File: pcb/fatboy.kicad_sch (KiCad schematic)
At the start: 76 parts, among them SW1 SW_Push, U1 Helios

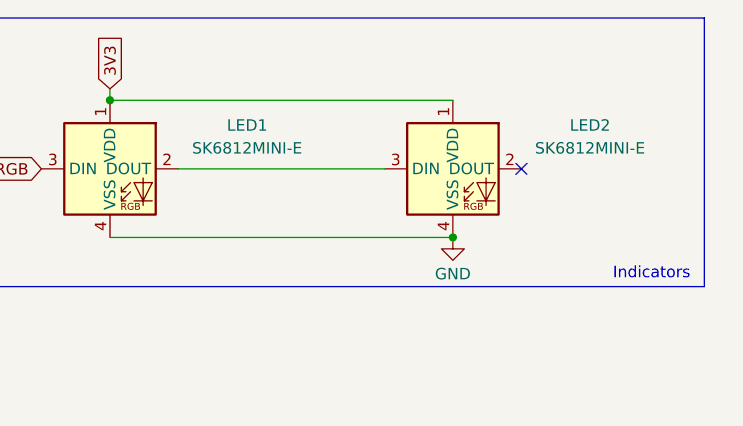
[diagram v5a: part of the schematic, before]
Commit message: update to use PCM_marbastlib:LED6028R
Signed-off-by: Anant Thazhemadam <anant.thazhemadam@gmail.com>
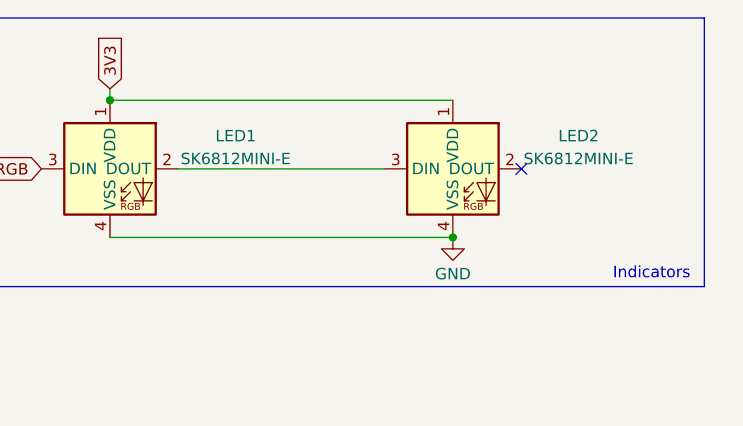
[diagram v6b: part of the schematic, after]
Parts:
- removed LED1, LED2: SK6812MINI-E, fatboy:LED_6028R, symbol marbastlib-various:SK6812MINI-E
- added LED1, LED2: SK6812MINI-E, PCM_marbastlib-various:LED_6028R, symbol PCM_marbastlib-various:SK6812MINI-E
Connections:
- net 3V3: now also LED1.1 (VDD), LED2.1 (VDD)
- net GND: now also LED1.4 (VSS), LED2.4 (VSS)
- net RGB: now also LED1.3 (DIN)
- new net: LED1.2 (DOUT), LED2.3 (DIN)
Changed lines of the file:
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@@
 	)
 	(junction
+		(at 160.02 36.83)
+		(diameter 0)
+		(color 0 0 0 0)
+	)
+	(junction
 		(at 107.95 171.45)
 		(diameter 0)
@@
 	)
 	(junction
-		(at 121.92 21.59)
-		(diameter 0)
-		(color 0 0 0 0)
-	)
-	(junction
 		(at 57.15 133.35)
 		(diameter 0)
@@
 	)
 	(junction
+		(at 121.92 21.59)
+		(diameter 0)
+		(color 0 0 0 0)
+	)
+	(junction
 		(at 120.65 190.5)
 		(diameter 0)
@@
 	)
 	(junction
-		(at 160.02 36.83)
-		(diameter 0)
-		(color 0 0 0 0)
-	)
-	(junction
 		(at 146.05 152.4)
 		(diameter 0)
@@
 	)
 	(no_connect
-		(at 167.64 29.21)
-	)
-	(no_connect
 		(at 50.8 31.75)
 	)
@@
 	)
 	(no_connect
+		(at 167.64 29.21)
+	)
+	(no_connect
 		(at 40.64 69.85)
 	)
@@
 	(wire
 		(pts
-			(xy 121.92 21.59) (xy 160.02 21.59)
-		)
-		(stroke
-			(width 0)
-			(type default)
-		)
-	)
-	(wire
-		(pts
 			(xy 57.15 190.5) (xy 69.85 190.5)
 		)
@@
 	(wire
 		(pts
-			(xy 121.92 36.83) (xy 160.02 36.83)
-		)
-		(stroke
-			(width 0)
-			(type default)
-		)
-	)
-	(wire
-		(pts
 			(xy 69.85 133.35) (xy 82.55 133.35)
 		)
@@
 	(wire
 		(pts
+			(xy 121.92 36.83) (xy 160.02 36.83)
+		)
+		(stroke
+			(width 0)
+			(type default)
+		)
+	)
+	(wire
+		(pts
 			(xy 44.45 133.35) (xy 57.15 133.35)
 		)
@@
 	(wire
 		(pts
+			(xy 129.54 29.21) (xy 152.4 29.21)
+		)
+		(stroke
+			(width 0)
+			(type default)
+		)
+	)
+	(wire
+		(pts
 			(xy 120.65 171.45) (xy 133.35 171.45)
 		)
@@
 	(wire
 		(pts
-			(xy 129.54 29.21) (xy 152.4 29.21)
+			(xy 153.67 114.3) (xy 153.67 120.65)
 		)
 		(stroke
@@
 	(wire
 		(pts
-			(xy 153.67 114.3) (xy 153.67 120.65)
+			(xy 133.35 152.4) (xy 146.05 152.4)
 		)
 		(stroke
@@
 	(wire
 		(pts
-			(xy 133.35 152.4) (xy 146.05 152.4)
+			(xy 57.15 133.35) (xy 69.85 133.35)
 		)
 		(stroke
@@
 	(wire
 		(pts
-			(xy 57.15 133.35) (xy 69.85 133.35)
+			(xy 121.92 21.59) (xy 160.02 21.59)
 		)
 		(stroke
@@
 	)
 	(symbol
+		(lib_id "PCM_marbastlib-various:SK6812MINI-E")
+		(at 160.02 29.21 0)
+		(unit 1)
+		(exclude_from_sim no)
+		(in_bom yes)
+		(on_board yes)
+		(dnp no)
+		(fields_autoplaced yes)
+		(property "Reference" "LED2"
+			(at 173.99 25.562 0)
+			(effects
+				(font
+					(size 1.27 1.27)
+				)
+			)
+		)
+		(property "Value" "SK6812MINI-E"
+			(at 173.99 28.102 0)
+			(effects
+				(font
+					(size 1.27 1.27)
+				)
+			)
+		)
+		(property "Footprint" "PCM_marbastlib-various:LED_6028R"
+			(at 160.02 29.21 0)
+			(effects
+				(font
+					(size 1.27 1.27)
+				)
+				(hide yes)
+			)
+		)
+		(property "Datasheet" ""
+			(at 160.02 29.21 0)
+			(effects
+				(font
+					(size 1.27 1.27)
+				)
+				(hide yes)
+			)
+		)
+		(property "Description" "Reverse mount adressable LED (WS2812 protocol)"
+			(at 160.02 29.21 0)
+			(effects
+				(font
+					(size 1.27 1.27)
+				)
+				(hide yes)
+			)
+		)
+		(pin "4"
+		)
+		(pin "1"
+		)
+		(pin "2"
+		)
+		(pin "3"
+		)
+		(instances
+			(project "fatboy"
+				(path "/ebfc642c-0c68-4d3e-b71f-85668561aa10"
+					(reference "LED2")
+					(unit 1)
+				)
+			)
+		)
+	)
+	(symbol
 		(lib_id "Diode:1N4148W")
 		(at 69.85 186.69 90)
@@
 	)
 	(symbol
-		(lib_id "marbastlib-various:SK6812MINI-E")
-		(at 160.02 29.21 0)
-		(unit 1)
-		(exclude_from_sim no)
-		(in_bom yes)
-		(on_board yes)
-		(dnp no)
-		(property "Reference" "LED2"
-			(at 175.26 24.384 0)
-			(effects
-				(font
-					(size 1.27 1.27)
-				)
-			)
-		)
-		(property "Value" "SK6812MINI-E"
-			(at 175.26 26.924 0)
-			(effects
-				(font
-					(size 1.27 1.27)
-				)
-			)
-		)
-		(property "Footprint" "fatboy:LED_6028R"
-			(at 160.02 29.21 0)
-			(effects
-				(font
-					(size 1.27 1.27)
-				)
-				(hide yes)
-			)
-		)
-		(property "Datasheet" ""
-			(at 160.02 29.21 0)
-			(effects
-				(font
-					(size 1.27 1.27)
-				)
-				(hide yes)
-			)
-		)
-		(property "Description" ""
-			(at 160.02 29.21 0)
-			(effects
-				(font
-					(size 1.27 1.27)
-				)
-				(hide yes)
-			)
-		)
-		(pin "2"
-		)
-		(pin "4"
-		)
-		(pin "1"
-		)
-		(pin "3"
-		)
-		(instances
-			(project "fatboy"
-				(path "/ebfc642c-0c68-4d3e-b71f-85668561aa10"
-					(reference "LED2")
-					(unit 1)
-				)
-			)
-		)
-	)
-	(symbol
 		(lib_id "PCM_marbastlib-mx:MX_SW_HS_CPG151101S11")
 		(at 54.61 142.24 0)
@@
 	)
 	(symbol
-		(lib_id "marbastlib-various:SK6812MINI-E")
-		(at 121.92 29.21 0)
-		(unit 1)
-		(exclude_from_sim no)
-		(in_bom yes)
-		(on_board yes)
-		(dnp no)
-		(property "Reference" "LED1"
-			(at 137.16 24.384 0)
-			(effects
-				(font
-					(size 1.27 1.27)
-				)
-			)
-		)
-		(property "Value" "SK6812MINI-E"
-			(at 137.16 26.924 0)
-			(effects
-				(font
-					(size 1.27 1.27)
-				)
-			)
-		)
-		(property "Footprint" "fatboy:LED_6028R"
-			(at 121.92 29.21 0)
-			(effects
-				(font
-					(size 1.27 1.27)
-				)
-				(hide yes)
-			)
-		)
-		(property "Datasheet" ""
-			(at 121.92 29.21 0)
-			(effects
-				(font
-					(size 1.27 1.27)
-				)
-				(hide yes)
-			)
-		)
-		(property "Description" ""
-			(at 121.92 29.21 0)
-			(effects
-				(font
-					(size 1.27 1.27)
-				)
-				(hide yes)
-			)
-		)
-		(pin "2"
-		)
-		(pin "4"
-		)
-		(pin "1"
-		)
-		(pin "3"
-		)
-		(instances
-			(project "fatboy"
-				(path "/ebfc642c-0c68-4d3e-b71f-85668561aa10"
-					(reference "LED1")
-					(unit 1)
-				)
-			)
-		)
-	)
-	(symbol
 		(lib_id "PCM_marbastlib-mx:MX_SW_HS_CPG151101S11")
 		(at 41.91 161.29 0)
@@
 					(unit 1)
 				)
+			)
+		)
+	)
+	(symbol
+		(lib_id "PCM_marbastlib-various:SK6812MINI-E")
+		(at 121.92 29.21 0)
+		(unit 1)
+		(exclude_from_sim no)
+		(in_bom yes)
+		(on_board yes)
+		(dnp no)
+		(fields_autoplaced yes)
+		(property "Reference" "LED1"
+			(at 135.89 25.562 0)
+			(effects
+				(font
+					(size 1.27 1.27)
+				)
+			)
+		)
+		(property "Value" "SK6812MINI-E"
+			(at 135.89 28.102 0)
+			(effects
+				(font
+					(size 1.27 1.27)
+				)
+			)
+		)
+		(property "Footprint" "PCM_marbastlib-various:LED_6028R"
+			(at 121.92 29.21 0)
+			(effects
+				(font
+					(size 1.27 1.27)
+				)
+				(hide yes)
+			)
+		)
+		(property "Datasheet" ""
+			(at 121.92 29.21 0)
+			(effects
+				(font
+					(size 1.27 1.27)
+				)
+				(hide yes)
+			)
+		)
+		(property "Description" "Reverse mount adressable LED (WS2812 protocol)"
+			(at 121.92 29.21 0)
+			(effects
+				(font
+					(size 1.27 1.27)
+				)
+				(hide yes)
+			)
+		)
+		(pin "4"
+		)
+		(pin "1"
+		)
+		(pin "2"
+		)
+		(pin "3"
+		)
+		(instances
+			(project "fatboy"
+				(path "/ebfc642c-0c68-4d3e-b71f-85668561aa10"
+					(reference "LED1")
+					(unit 1)
+				)

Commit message: update helios footprint
Signed-off-by: Anant Thazhemadam <anant.thazhemadam@gmail.com>
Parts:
- removed U1: Helios, PCM_marbastlib-xp-promicroish:Helios_ACH, symbol marbastlib-promicroish:Helios
- added U1: Helios, PCM_marbastlib-xp-promicroish:Helios_AH_USBup, symbol PCM_marbastlib-promicroish:Helios
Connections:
- net 3V3: now also U1.16 (3V3)
- net 5V: now also U1.13 (5V)
- net COL1: now also U1.21 (P22)
- net COL10: now also U1.9 (P6)
- net COL2: now also U1.20 (P26)
- net COL3: now also U1.19 (P27)
- net COL4: now also U1.18 (P28)
- net COL5: now also U1.17 (P29)
- net COL6: now also U1.5 (P2)
- net COL7: now also U1.6 (P3)
- net COL8: now also U1.7 (P4)
- net COL9: now also U1.8 (P5)
- net GND: now also U1.14 (GND), U1.3 (GND), U1.4 (GND)
- net RESET: now also U1.15 (RST)
- net RGB: now also U1.29 (P16)
- net ROW1: now also U1.10 (P7)
- net ROW2: now also U1.11 (P8)
- net ROW3: now also U1.12 (P9)
- net ROW4: now also U1.25 (P12)
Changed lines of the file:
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@@
+	)
+	(symbol
+		(lib_id "PCM_marbastlib-promicroish:Helios")
+		(at 38.1 48.26 0)
+		(unit 1)
+		(exclude_from_sim no)
+		(in_bom no)
+		(on_board yes)
+		(dnp no)
+		(fields_autoplaced yes)
+		(property "Reference" "U1"
+			(at 41.5641 24.13 0)
+			(effects
+				(font
+					(size 1.27 1.27)
+				)
+				(justify left)
+			)
+		)
+		(property "Value" "Helios"
+			(at 41.5641 26.67 0)
+			(effects
+				(font
+					(size 1.27 1.27)
+				)
+				(justify left)
+			)
+		)
+		(property "Footprint" "PCM_marbastlib-xp-promicroish:Helios_AH_USBup"
+			(at 38.1 72.39 0)
+			(effects
+				(font
+					(size 1.27 1.27)
+				)
+				(hide yes)
+			)
+		)
+		(property "Datasheet" "https://github.com/0xCB-dev/0xCB-Helios"
+			(at 38.1 74.93 0)
+			(effects
+				(font
+					(size 1.27 1.27)
+				)
+				(hide yes)
+			)
+		)
+		(property "Description" "Symbol for an 0xCB Helios"
+			(at 38.1 48.26 0)
+			(effects
+				(font
+					(size 1.27 1.27)
+				)
+				(hide yes)
+			)
+		)
+		(pin "10"
+		)
+		(pin "17"
+		)
+		(pin "21"
+		)
+		(pin "22"
+		)
+		(pin "2"
+		)
+		(pin "20"
+		)
+		(pin "18"
+		)
+		(pin "14"
+		)
+		(pin "12"
+		)
+		(pin "5"
+		)
+		(pin "6"
+		)
+		(pin "26"
+		)
+		(pin "27"
+		)
+		(pin "28"
+		)
+		(pin "29"
+		)
+		(pin "30"
+		)
+		(pin "31"
+		)
+		(pin "32"
+		)
+		(pin "33"
+		)
+		(pin "34"
+		)
+		(pin "11"
+		)
+		(pin "19"
+		)
+		(pin "23"
+		)
+		(pin "24"
+		)
+		(pin "3"
+		)
+		(pin "4"
+		)
+		(pin "1"
+		)
+		(pin "9"
+		)
+		(pin "13"
+		)
+		(pin "16"
+		)
+		(pin "25"
+		)
+		(pin "15"
+		)
+		(pin "7"
+		)
+		(pin "8"
+		)
+		(instances
+			(project "fatboy"
+				(path "/ebfc642c-0c68-4d3e-b71f-85668561aa10"
+					(reference "U1")
+					(unit 1)
+				)
+			)
+		)
 	)
 	(symbol
@@
 					(unit 1)
 				)
-			)
-		)
-	)
-	(symbol
-		(lib_id "marbastlib-promicroish:Helios")
-		(at 38.1 48.26 0)
-		(unit 1)
-		(exclude_from_sim yes)
-		(in_bom no)
-		(on_board yes)
-		(dnp no)
-		(fields_autoplaced yes)
-		(property "Reference" "U1"
-			(at 41.5641 24.13 0)
-			(effects
-				(font
-					(size 1.27 1.27)
-				)
-				(justify left)
-			)
-		)
-		(property "Value" "Helios"
-			(at 41.5641 26.67 0)
-			(effects
-				(font
-					(size 1.27 1.27)
-				)
-				(justify left)
-			)
-		)
-		(property "Footprint" "PCM_marbastlib-xp-promicroish:Helios_ACH"
-			(at 38.1 72.39 0)
-			(effects
-				(font
-					(size 1.27 1.27)
-				)
-				(hide yes)
-			)
-		)
-		(property "Datasheet" "https://github.com/0xCB-dev/0xCB-Helios"
-			(at 38.1 74.93 0)
-			(effects
-				(font
-					(size 1.27 1.27)
-				)
-				(hide yes)
-			)
-		)
-		(property "Description" ""
-			(at 38.1 48.26 0)
-			(effects
-				(font
-					(size 1.27 1.27)
-				)
-				(hide yes)
-			)
-		)
-		(pin "22"
-		)
-		(pin "8"
-		)
-		(pin "25"
-		)
-		(pin "28"
-		)
-		(pin "4"
-		)
-		(pin "27"
-		)
-		(pin "17"
-		)
-		(pin "18"
-		)
-		(pin "1"
-		)
-		(pin "11"
-		)
-		(pin "15"
-		)
-		(pin "34"
-		)
-		(pin "26"
-		)
-		(pin "23"
-		)
-		(pin "16"
-		)
-		(pin "29"
-		)
-		(pin "19"
-		)
-		(pin "33"
-		)
-		(pin "31"
-		)
-		(pin "24"
-		)
-		(pin "20"
-		)
-		(pin "9"
-		)
-		(pin "13"
-		)
-		(pin "5"
-		)
-		(pin "21"
-		)
-		(pin "32"
-		)
-		(pin "6"
-		)
-		(pin "2"
-		)
-		(pin "7"
-		)
-		(pin "3"
-		)
-		(pin "30"
-		)
-		(pin "10"
-		)
-		(pin "14"
-		)
-		(pin "12"
-		)
-		(instances
-			(project "fatboy"
-				(path "/ebfc642c-0c68-4d3e-b71f-85668561aa10"
-					(reference "U1")
-					(unit 1)
-				)

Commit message: update reset switch footprint
Signed-off-by: Anant Thazhemadam <anant.thazhemadam@gmail.com>
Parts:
- SW1: footprint fatboy:top_reset -> PCM_marbastlib-various:SW_SKHLLCA010
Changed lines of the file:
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@@
 			)
 		)
-		(property "Footprint" "fatboy:top_reset"
+		(property "Footprint" "PCM_marbastlib-various:SW_SKHLLCA010"
 			(at 86.36 21.59 0)
 			(effects
